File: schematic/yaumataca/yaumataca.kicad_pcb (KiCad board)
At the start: 2 copper layers, 33 parts, among them J1 Joystick Port, J2 Mouse Port, J3 Conn_02x05_Odd_Even, J4 Conn_02x05_Odd_Even, Q1 BC547, Q10 BC547, Q11 BC547, Q12 BC547, Q13 BC547, Q14 BC547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

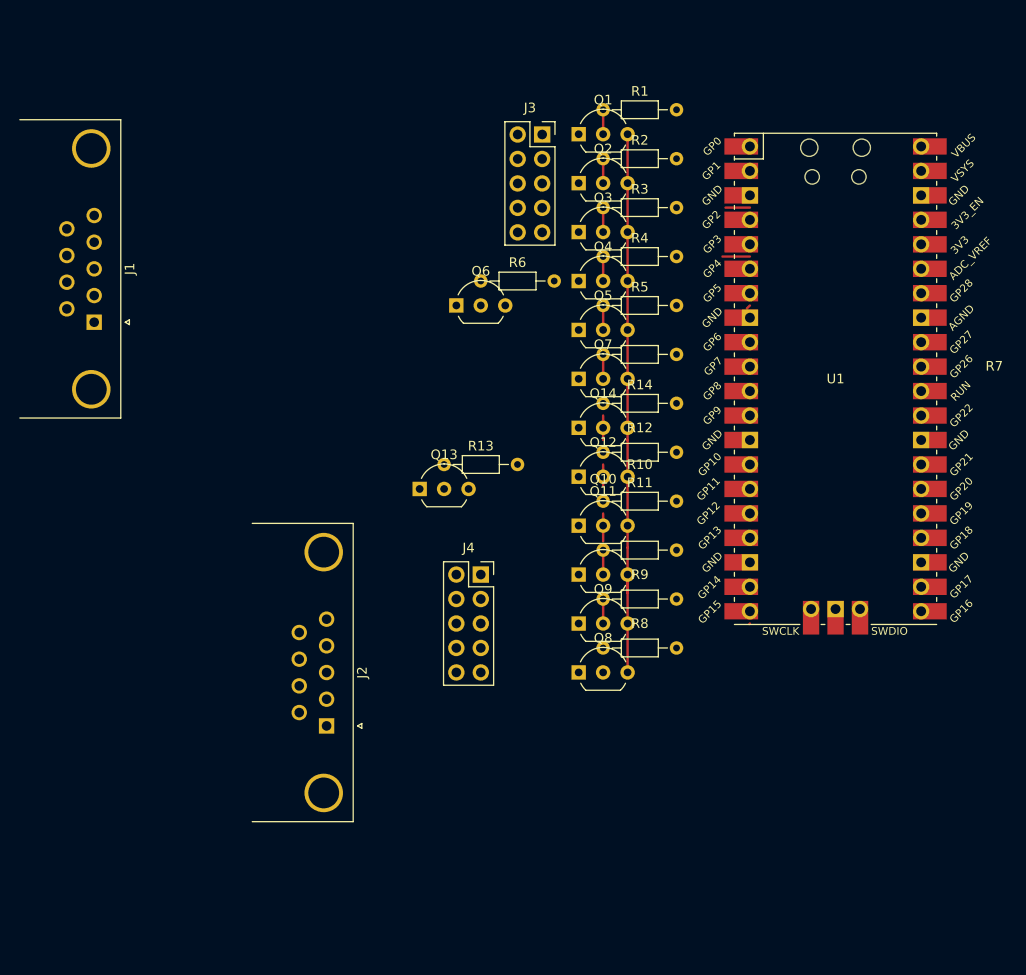
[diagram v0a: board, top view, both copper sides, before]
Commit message: Documentation
Just a little bit more text.
Also updated schematics and created
some diagrams.
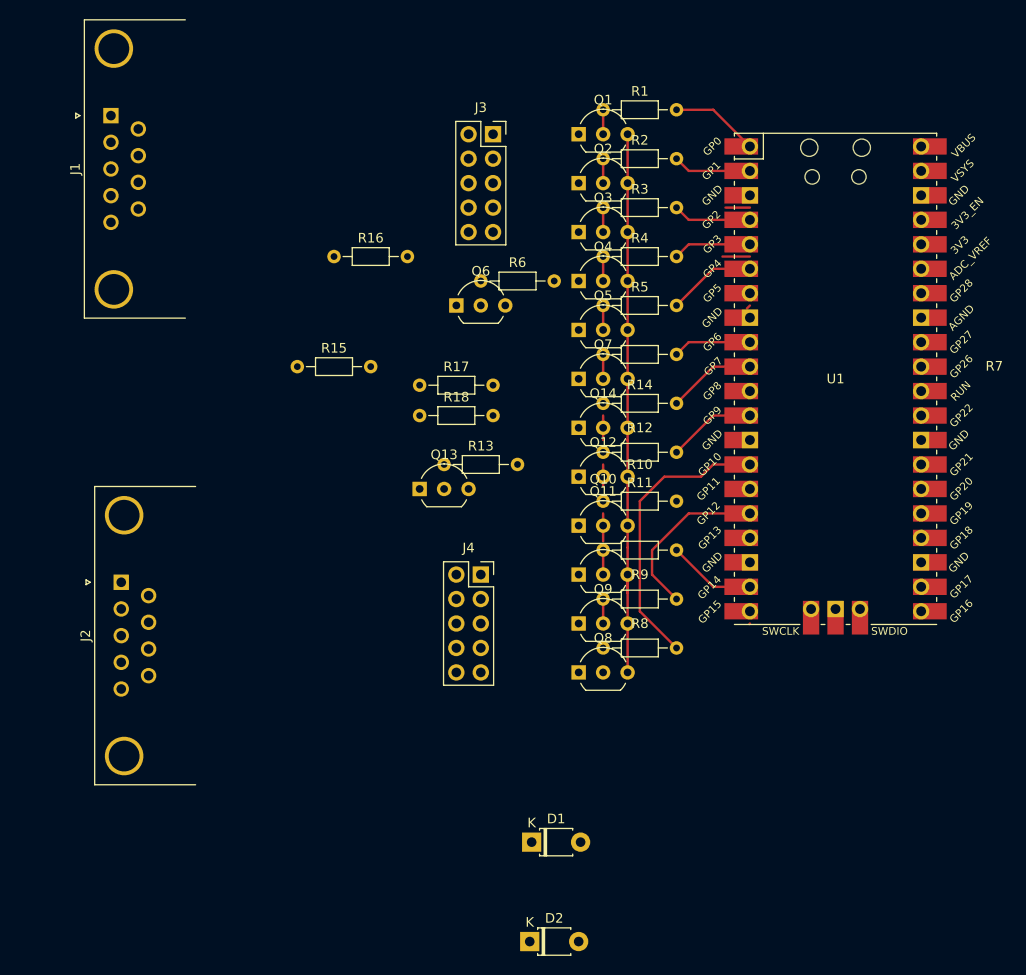
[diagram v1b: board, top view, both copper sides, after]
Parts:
- added D1: D, Diode_THT:D_T-1_P5.08mm_Horizontal, F.Cu at (145.0, 137.0)
- added D2: D, Diode_THT:D_T-1_P5.08mm_Horizontal, F.Cu at (144.8, 147.3)
- added R15: 10k, Resistor_THT:R_Axial_DIN0204_L3.6mm_D1.6mm_P7.62mm_Horizontal, F.Cu at (120.7, 87.6)
- added R16: 10k, Resistor_THT:R_Axial_DIN0204_L3.6mm_D1.6mm_P7.62mm_Horizontal, F.Cu at (124.5, 76.2)
- added R17: 10k, Resistor_THT:R_Axial_DIN0204_L3.6mm_D1.6mm_P7.62mm_Horizontal, F.Cu at (133.3, 89.6)
- added R18: 10k, Resistor_THT:R_Axial_DIN0204_L3.6mm_D1.6mm_P7.62mm_Horizontal, F.Cu at (133.3, 92.7)
- moved J2 26.0 mm to (102.4, 110.0), turned to 90 degrees
- moved J1 21.5 mm to (101.3, 61.6), turned to 90 degrees
- moved J3 5.10 mm to (141.0, 63.5)
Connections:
- net /Joystick_Down renamed /Pi_Joystick_Down
- net /Joystick_Fire1 renamed /Pi_Joystick_Fire1
- net /Joystick_Fire2 renamed /Pi_Joystick_Fire2
- net /Joystick_Fire3 renamed /Pi_Joystick_Fire3
- net /Joystick_Left renamed /Pi_Joystick_Left
- net /Joystick_Right renamed /Pi_Joystick_Right
- net /Joystick_Up renamed /Pi_Joystick_Up
- net Net-(J3-Pin_5) renamed /Joy_Left
- J1 pad 1: Net-(J3-Pin_9) -> /Joy_Up
- J1 pad 2: Net-(J3-Pin_7) -> /Joy_Down
- J1 pad 4: Net-(J3-Pin_3) -> /Joy_Right
- J1 pad 5: Net-(J3-Pin_1) -> /Joy_Fire3
- J1 pad 6: Net-(J3-Pin_10) -> /Joy_Fire1
- J1 pad 9: Net-(J3-Pin_4) -> /Joy_Fire2
- J2 pad 1: Net-(J4-Pin_9) -> /Mouse_Up
- J2 pad 2: Net-(J4-Pin_7) -> /Mouse_Down
- J2 pad 3: Net-(J4-Pin_5) -> /Mouse_Left
- J2 pad 4: Net-(J4-Pin_3) -> /Mouse_Right
- J2 pad 5: Net-(J4-Pin_1) -> /Mouse_Fire3
- J2 pad 6: Net-(J4-Pin_10) -> /Mouse_Fire1
- J2 pad 9: Net-(J4-Pin_4) -> /Mouse_Fire2
- J3 pad 1: Net-(J3-Pin_1) -> /Joy_Up
- J3 pad 10: Net-(J3-Pin_10) -> unconnected-(J3-Pin_10-Pad10)
- J3 pad 2: unconnected-(J3-Pin_2-Pad2) -> /Joy_Fire1
- J3 pad 3: Net-(J3-Pin_3) -> /Joy_Down
- J3 pad 4: Net-(J3-Pin_4) -> +5V
- J3 pad 7: Net-(J3-Pin_7) -> /Joy_Right
- J3 pad 8: +5V -> /Joy_Fire2
- J3 pad 9: Net-(J3-Pin_9) -> /Joy_Fire3
- J4 pad 1: Net-(J4-Pin_1) -> /Mouse_Up
- J4 pad 10: Net-(J4-Pin_10) -> unconnected-(J4-Pin_10-Pad10)
- J4 pad 2: unconnected-(J4-Pin_2-Pad2) -> /Mouse_Fire1
- J4 pad 3: Net-(J4-Pin_3) -> /Mouse_Down
- J4 pad 4: Net-(J4-Pin_4) -> +5V
- J4 pad 5: Net-(J4-Pin_5) -> /Mouse_Left
- J4 pad 7: Net-(J4-Pin_7) -> /Mouse_Right
- J4 pad 8: +5V -> /Mouse_Fire2
- J4 pad 9: Net-(J4-Pin_9) -> /Mouse_Fire3
- Q1 pad 1: Net-(J3-Pin_3) -> /Joy_Right
- Q10 pad 1: Net-(J4-Pin_7) -> /Mouse_Down
- Q11 pad 1: Net-(J4-Pin_9) -> /Mouse_Up
- Q12 pad 1: Net-(J4-Pin_10) -> /Mouse_Fire1
- Q13 pad 1: Net-(J4-Pin_1) -> /Mouse_Fire3
- Q14 pad 1: Net-(J4-Pin_4) -> /Mouse_Fire2
- Q3 pad 1: Net-(J3-Pin_7) -> /Joy_Down
- Q4 pad 1: Net-(J3-Pin_9) -> /Joy_Up
- Q5 pad 1: Net-(J3-Pin_10) -> /Joy_Fire1
- Q6 pad 1: Net-(J3-Pin_1) -> /Joy_Fire3
- Q7 pad 1: Net-(J3-Pin_4) -> /Joy_Fire2
- Q8 pad 1: Net-(J4-Pin_3) -> /Mouse_Right
- Q9 pad 1: Net-(J4-Pin_5) -> /Mouse_Left
- R10 pad 2: /Mouse_Down -> /Pi_Mouse_Down
- R11 pad 2: /Mouse_Up -> /Pi_Mouse_Up
- R12 pad 2: /Mouse_Fire1 -> /Pi_Mouse_Fire1
- R13 pad 2: /Mouse_Fire3 -> /Pi_Mouse_Fire3
- R14 pad 2: /Mouse_Fire2 -> /Pi_Mouse_Fire2
- R8 pad 2: /Mouse_Right -> /Pi_Mouse_Right
- R9 pad 2: /Mouse_Left -> /Pi_Mouse_Left
- U1 pad 10: /Mouse_Fire2 -> /Pi_Mouse_Fire2
- U1 pad 11: unconnected-(U1-GPIO8-Pad11) -> /Joystick_Pot_Sense
- U1 pad 12: /Mouse_Fire1 -> /Pi_Mouse_Fire1
- U1 pad 13: unconnected-(U1-GND-Pad13) -> GND
- U1 pad 14: /Mouse_Up -> /Pi_Mouse_Right
- U1 pad 15: /Mouse_Fire3 -> /Pi_Mouse_Fire3
- U1 pad 16: /Mouse_Down -> /Pi_Mouse_Left
- U1 pad 17: unconnected-(U1-GPIO13-Pad17) -> /Mouse_Pot_Sense
- U1 pad 18: unconnected-(U1-GND-Pad18) -> GND
- U1 pad 19: /Mouse_Left -> /Pi_Mouse_Down
- U1 pad 20: /Mouse_Right -> /Pi_Mouse_Up
- U1 pad 3: unconnected-(U1-GND-Pad3) -> GND
- U1 pad 8: unconnected-(U1-GND-Pad8) -> GND
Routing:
- net /Pi_Mouse_Right: track 0.00 -> 29.8 mm
- net /Pi_Mouse_Left: track 0.00 -> 17.9 mm
- net /Pi_Joystick_Right: track 0.00 -> 9.20 mm
- net /Pi_Mouse_Fire2: track 0.00 -> 9.20 mm
- net /Pi_Mouse_Fire1: track 0.00 -> 9.20 mm
- net /Pi_Joystick_Fire1: track 0.00 -> 9.20 mm
- net /Pi_Mouse_Down: track 0.00 -> 9.20 mm
- net /Pi_Joystick_Up: track 0.00 -> 8.15 mm
- net /Pi_Joystick_Fire2: track 0.00 -> 8.15 mm
- net /Pi_Joystick_Left: track 2.54 -> 8.15 mm
- net (no net): track 0.00 -> 5.39 mm
- net /Pi_Joystick_Down: track 2.85 -> 8.15 mm

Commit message: First idea of a PCB
All components on one side
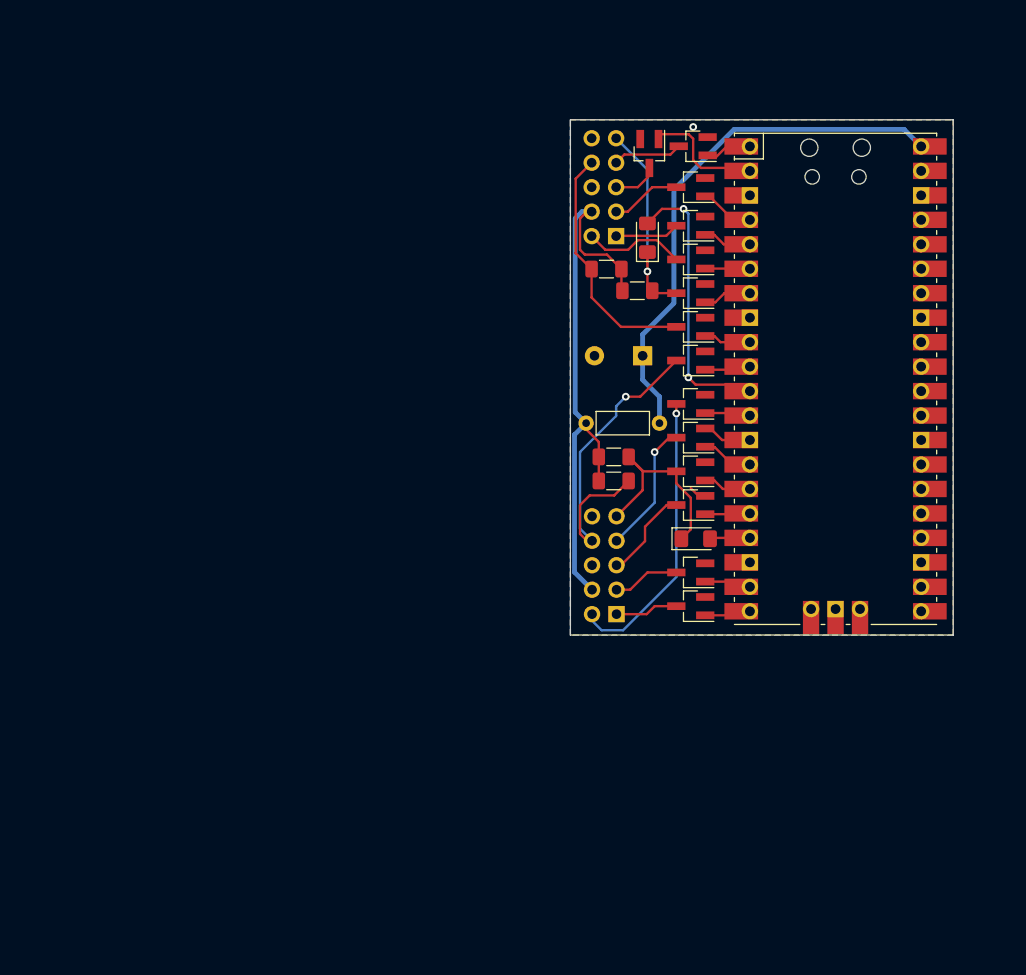
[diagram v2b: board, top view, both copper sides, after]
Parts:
- removed J1: Joystick Port, Connector_Dsub:DSUB-9_Female_Horizontal_P2.77x2.84mm_EdgePinOffset4.94mm_Housed_MountingHolesOffset7.48mm
- removed J2: Mouse Port, Connector_Dsub:DSUB-9_Female_Horizontal_P2.77x2.84mm_EdgePinOffset4.94mm_Housed_MountingHolesOffset7.48mm
- removed R1, R10, R11, R12, R13, R14, R2, R3, R4, R5, R6, R7, R8, R9: 10k, Resistor_THT:R_Axial_DIN0204_L3.6mm_D1.6mm_P7.62mm_Horizontal
- added C1: C_Polarized, Capacitor_THT:CP_Radial_D10.0mm_P5.00mm, F.Cu at (156.5, 86.5)
- added L1: L_Ferrite, Inductor_THT:L_Axial_L5.3mm_D2.2mm_P7.62mm_Horizontal_Vishay_IM-1, F.Cu at (158.2, 93.5)
- D1, D2: footprint Diode_THT:D_T-1_P5.08mm_Horizontal -> Diode_SMD:D_1206_3216Metric_Pad1.42x1.75mm_HandSolder
- J3, J4: moved to B.Cu
- Q1, Q10, Q11, Q12, Q13, Q14, Q2, Q3, Q4, Q5, Q6, Q7, Q8, Q9: value BC547 -> DTC143Z; footprint Package_TO_SOT_THT:TO-92_Inline_Wide -> Package_TO_SOT_SMD:SOT-23_Handsoldering
- R15, R16, R17, R18: footprint Resistor_THT:R_Axial_DIN0204_L3.6mm_D1.6mm_P7.62mm_Horizontal -> Resistor_SMD:R_1206_3216Metric_Pad1.30x1.75mm_HandSolder
- moved D2 74.1 mm to (157.0, 74.2), turned to 90 degrees
- moved D1 35.8 mm to (162.0, 105.5)
- moved Q8 34.4 mm to (161.5, 87.0), turned to 180 degrees
- moved R15 34.2 mm to (153.5, 97.0), turned to 180 degrees
- moved R16 31.7 mm to (155.9, 79.8), turned to 180 degrees
- moved Q13 28.2 mm to (161.5, 102.0), turned to 180 degrees
- moved Q6 24.4 mm to (161.5, 80.0), turned to 180 degrees
- moved R17 22.8 mm to (152.8, 77.5)
- moved R18 21.3 mm to (153.5, 99.5), turned to 180 degrees
- moved Q10 21.2 mm to (161.5, 91.5), turned to 180 degrees
- moved Q9 19.6 mm to (161.5, 98.5), turned to 180 degrees
- moved J3 16.6 mm to (153.8, 74.1)
- moved Q12 15.3 mm to (161.5, 109.0), turned to 180 degrees
- moved J4 14.7 mm to (153.8, 113.3)
- moved Q11 14.3 mm to (161.5, 112.5), turned to 180 degrees
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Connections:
- Q1 pad 1: /Joy_Right -> /Pi_Joystick_Right
- Q1 pad 2: Net-(Q1-B) -> GND
- Q1 pad 3: GND -> /Joy_Right
- Q10 pad 1: /Mouse_Down -> /Pi_Mouse_Fire1
- Q10 pad 2: Net-(Q10-B) -> GND
- Q10 pad 3: GND -> /Mouse_Fire1
- Q11 pad 1: /Mouse_Up -> /Pi_Mouse_Up
- Q11 pad 2: Net-(Q11-B) -> GND
- Q11 pad 3: GND -> /Mouse_Up
- Q12 pad 1: /Mouse_Fire1 -> /Pi_Mouse_Down
- Q12 pad 2: Net-(Q12-B) -> GND
- Q12 pad 3: GND -> /Mouse_Down
- Q13 pad 1: /Mouse_Fire3 -> /Pi_Mouse_Left
- Q13 pad 2: Net-(Q13-B) -> GND
- Q13 pad 3: GND -> /Mouse_Left
- Q14 pad 1: /Mouse_Fire2 -> /Pi_Mouse_Right
- Q14 pad 2: Net-(Q14-B) -> GND
- Q14 pad 3: GND -> /Mouse_Right
- Q2 pad 1: /Joy_Left -> /Pi_Joystick_Left
- Q2 pad 2: Net-(Q2-B) -> GND
- Q2 pad 3: GND -> /Joy_Left
- Q3 pad 1: /Joy_Down -> /Pi_Joystick_Down
- Q3 pad 2: Net-(Q3-B) -> GND
- Q3 pad 3: GND -> /Joy_Down
- Q4 pad 1: /Joy_Up -> /Pi_Joystick_Up
- Q4 pad 2: Net-(Q4-B) -> GND
- Q4 pad 3: GND -> /Joy_Up
- Q5 pad 1: /Joy_Fire1 -> /Pi_Joystick_Fire1
- Q5 pad 2: Net-(Q5-B) -> GND
- Q5 pad 3: GND -> /Joy_Fire1
- Q6 pad 1: /Joy_Fire3 -> /Pi_Joystick_Fire3
- Q6 pad 2: Net-(Q6-B) -> GND
- Q6 pad 3: GND -> /Joy_Fire3
- Q7 pad 1: /Joy_Fire2 -> /Pi_Joystick_Fire2
- Q7 pad 2: Net-(Q7-B) -> GND
- Q7 pad 3: GND -> /Joy_Fire2
- Q8 pad 1: /Mouse_Right -> /Pi_Mouse_Fire2
- Q8 pad 2: Net-(Q8-B) -> GND
- Q8 pad 3: GND -> /Mouse_Fire2
- Q9 pad 1: /Mouse_Left -> /Pi_Mouse_Fire3
- Q9 pad 2: Net-(Q9-B) -> GND
- Q9 pad 3: GND -> /Mouse_Fire3
- U1 pad 40: +5V -> Net-(U1-VBUS)
- U1 pad 42: unconnected-(U1-GND-Pad42) -> GND
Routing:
- net +5V: track 0.00 -> 60.5 mm
- net Net-(U1-VBUS): track 0.00 -> 55.3 mm
- net GND: track 58.6 -> 6.27 mm, vias 0 -> 1
- net /Mouse_Fire2: track 0.00 -> 34.9 mm, vias 0 -> 1
- net /Mouse_Fire1: track 0.00 -> 30.1 mm, vias 0 -> 1
- net /Joystick_Pot_Sense: track 0.00 -> 29.1 mm, vias 0 -> 2
- net /Joy_Fire2: track 0.00 -> 25.4 mm
- net /Pi_Mouse_Right: track 29.8 -> 5.43 mm
- net /Joy_Fire3: track 0.00 -> 22.0 mm, vias 0 -> 1
- net /Mouse_Fire3: track 0.00 -> 21.5 mm
- net /Mouse_Right: track 0.00 -> 13.7 mm, vias 0 -> 1
- net /Pi_Mouse_Left: track 17.9 -> 4.67 mm
- net /Joy_Fire1: track 0.00 -> 10.6 mm
- net /Mouse_Left: track 0.10 -> 9.68 mm
- net /Joy_Down: track 0.00 -> 7.30 mm
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- added copper zone on B.Cu, net GND
- added copper zone on F.Cu, net GND
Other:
- board outline added: 39.8 x 53.5 mm

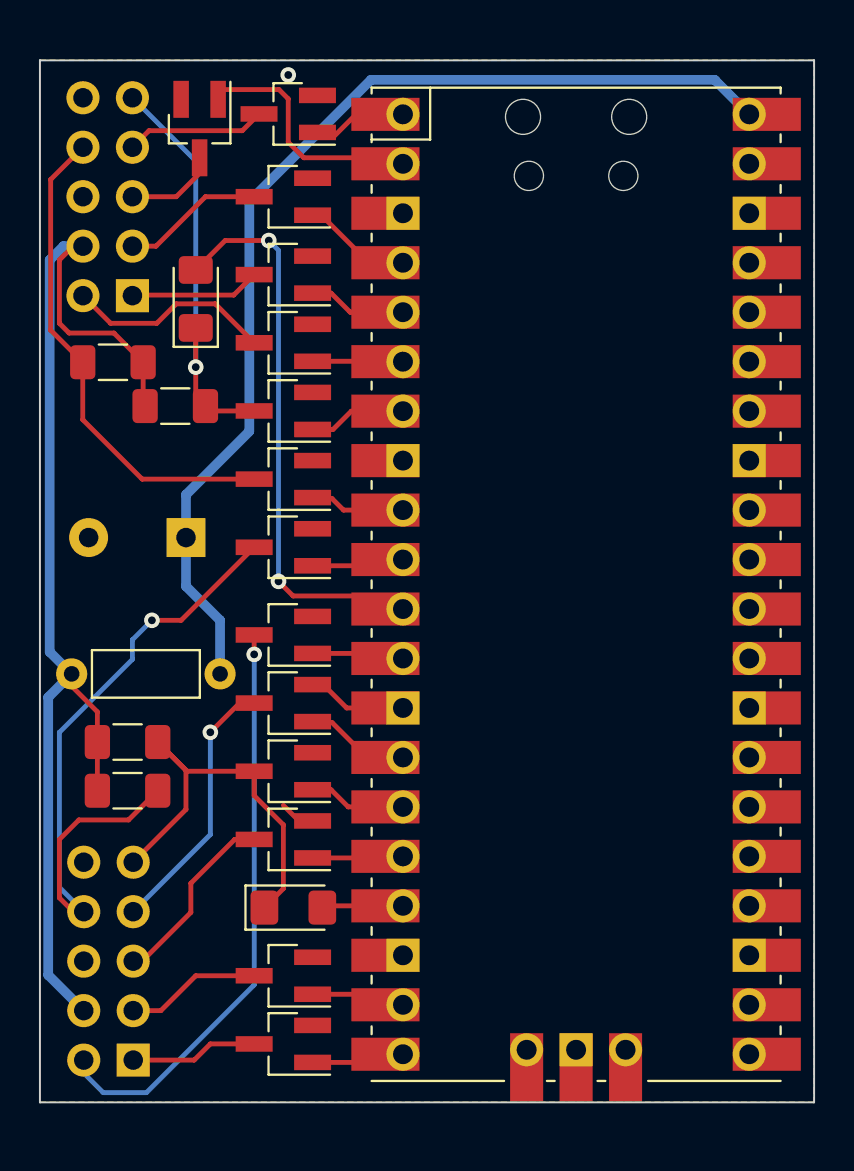
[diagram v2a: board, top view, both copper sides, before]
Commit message: Added ordered PCB
Components on both sides for an
even smaller size.
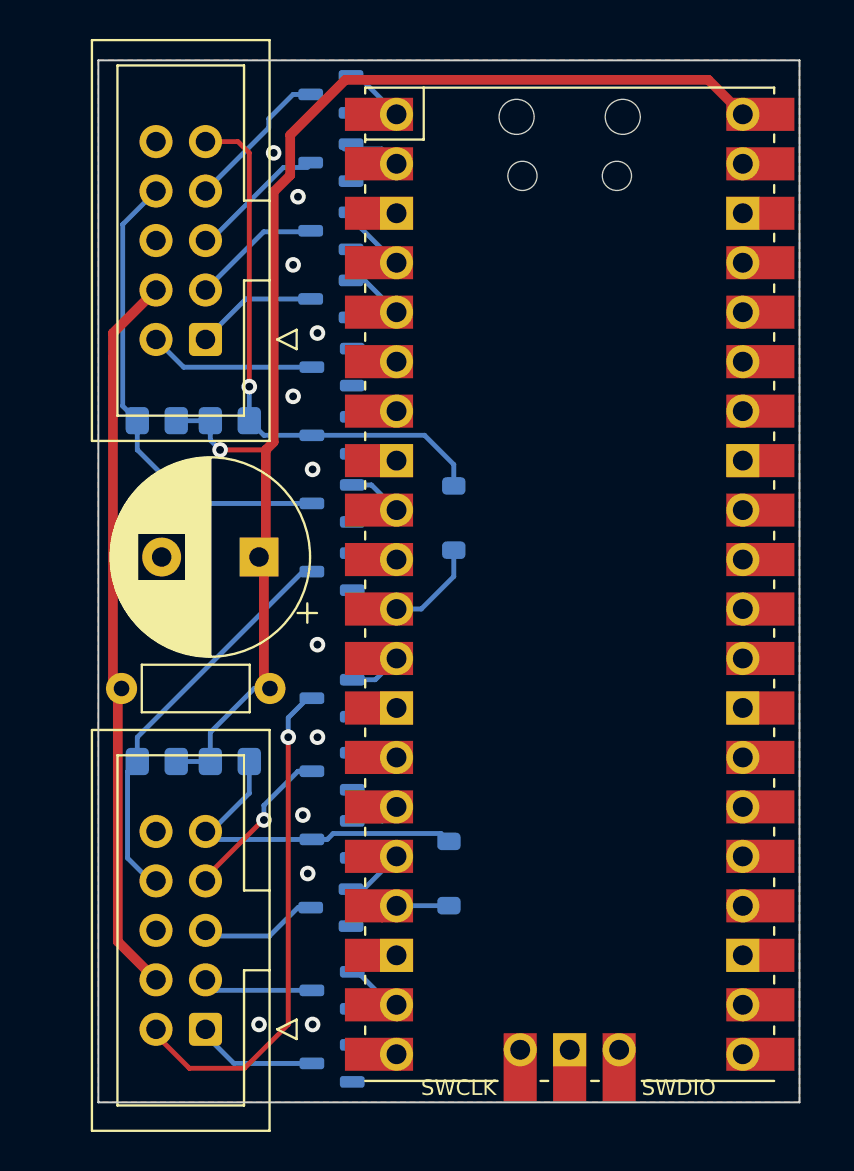
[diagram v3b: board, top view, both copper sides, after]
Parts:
- C1: value C_Polarized -> 1000u
- D1, D2: footprint Diode_SMD:D_1206_3216Metric_Pad1.42x1.75mm_HandSolder -> Diode_SMD:D_SOD-123; moved to B.Cu
- J3, J4: footprint Connector_PinSocket_2.54mm:PinSocket_2x05_P2.54mm_Vertical -> Connector_IDC:IDC-Header_2x05_P2.54mm_Vertical; moved to F.Cu
- L1: value L_Ferrite -> 100u
- Q1, Q10, Q11, Q12, Q13, Q14, Q2, Q3, Q4, Q5, Q6, Q7, Q8, Q9: footprint Package_TO_SOT_SMD:SOT-23_Handsoldering -> Library:SOT-23_ohnesilk; moved to B.Cu
- R15, R16, R17, R18: footprint Resistor_SMD:R_1206_3216Metric_Pad1.30x1.75mm_HandSolder -> Resistor_SMD:R_0805_2012Metric_Pad1.20x1.40mm_HandSolder; moved to B.Cu
- moved D2 17.4 mm to (170.2, 85.5), turned to -90 degrees
- moved D1 8.18 mm to (170.0, 103.8), turned to -90 degrees
- moved Q2 6.96 mm to (163.9, 67.2), turned to 180 degrees
- moved R15 5.34 mm to (158.8, 98.0)
- moved J3 4.37 mm to (157.5, 76.3), turned to 180 degrees
- moved Q14 4.30 mm to (164.0, 98.5)
- moved Q9 4.30 mm to (164.0, 102.0)
- moved Q13 4.27 mm to (163.9, 105.5)
- moved Q10 4.10 mm to (164.0, 94.8)
- moved J4 4.03 mm to (157.5, 111.8), turned to 180 degrees
- moved C1 3.88 mm to (160.2, 87.5)
- moved R17 3.75 mm to (155.0, 80.5)
- moved Q3 3.00 mm to (163.9, 70.8)
- moved R16 2.90 mm to (158.8, 80.5)
- moved Q5 2.80 mm to (164.0, 77.8)
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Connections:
- C1 pad 1: Net-(U1-VBUS) -> +5V
- J3 pad 4: +5V -> /HOST_5V
- J4 pad 4: +5V -> /HOST_5V
- L1 pad 1: Net-(U1-VBUS) -> +5V
- L1 pad 2: +5V -> /HOST_5V
- U1 pad 40: Net-(U1-VBUS) -> +5V
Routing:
- net Net-(U1-VBUS): track 55.3 -> 0.00 mm
- net /HOST_5V: track 0.00 -> 37.4 mm
- net /Joystick_Pot_Sense: track 29.1 -> 5.09 mm, vias 2 -> 0
- net /Mouse_Fire2: track 34.9 -> 21.1 mm, vias 1 -> 0
- net /Pi_Joystick_Left: track 12.3 -> 3.00 mm
- net +5V: track 60.5 -> 67.5 mm, vias 0 -> 1
- net /Joy_Fire3: track 22.0 -> 28.9 mm
- net GND: track 6.27 -> 0.00 mm, vias 1 -> 12
- net /Mouse_Right: track 13.7 -> 8.72 mm
- net /Mouse_Fire1: track 30.1 -> 25.9 mm
- net /Mouse_Fire3: track 21.5 -> 17.7 mm
- net /Mouse_Left: track 9.68 -> 6.10 mm
- net /Pi_Mouse_Right: track 5.43 -> 2.18 mm
- net /Pi_Joystick_Fire3: track 5.03 -> 2.49 mm
- net /Pi_Mouse_Fire3: track 5.00 -> 2.67 mm
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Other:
- board size 39.8 x 53.5 mm -> 36 x 53.5 mm

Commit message: Added revision silkscreen
It was missing from the order.
No other change to the circuit
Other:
- board text added: "Yaumataca Rev 0.1 Designed by Slamy"
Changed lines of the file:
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@@
   (gr_rect (start 152 62) (end 188 115.5)
     (stroke (width 0.1) (type default)) (fill none) (layer "Edge.Cuts"))
+  (gr_text "Yaumataca Rev 0.1\nDesigned by Slamy" (at 181.5 94 90) (layer "B.SilkS")
+    (effects (font (size 1.5 1.5) (thickness 0.3) bold) (justify right bottom mirror))
+  )
   (dimension (type orthogonal) (layer "Dwgs.User")
     (pts (xy 152 62) (xy 188 62))
